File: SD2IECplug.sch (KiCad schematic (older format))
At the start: 46 parts, among them J1 ISP, J2 LED/SW, J3 SD_Card, J4 IEC, J5 C64-CassettePort, J6 C64-CassettePort, J7 USB_B, Q1 IRLML2803, Q2 IRLML2803, Q3 IRLML2803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

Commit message: Added optional I2C connector.
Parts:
- added J8: I2C, Pin_Headers:Pin_Header_Straight_1x04_Pitch2.54mm, symbol Conn_01x04
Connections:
- net labels added: SCL, SDA
- wire segments 111 -> 118
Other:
- moved on the sheet: D1, D2, J2, R1, R5

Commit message: Removed push button, added switch header.
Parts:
- removed SW1: DiskSwitch, Buttons_Switches_THT:SW_PUSH_6mm, symbol SW_Push
- added J9: SW, Pin_Headers:Pin_Header_Straight_1x06_Pitch2.54mm, symbol Conn_01x06
- J2: value LED/SW -> LED; symbol Conn_01x04 -> Conn_01x03
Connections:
- wire segments 118 -> 157
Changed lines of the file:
@@
 L GND #PWR017
 U 1 1 5A0E601A
-P 5250 4850
-F 0 "#PWR017" H 5250 4600 50  0001 C CNN
-F 1 "GND" H 5250 4700 50  0000 C CNN
-F 2 "" H 5250 4850 50  0001 C CNN
-F 3 "" H 5250 4850 50  0001 C CNN
-	1    5250 4850
-	1    0    0    -1
-$EndComp
-$Comp
-L SW_Push SW1
-U 1 1 5A0E643C
-P 4200 4800
-F 0 "SW1" H 4250 4900 50  0000 L CNN
-F 1 "DiskSwitch" H 4200 4740 50  0000 C CNN
-F 2 "Buttons_Switches_THT:SW_PUSH_6mm" H 4200 5000 50  0001 C CNN
-F 3 "" H 4200 5000 50  0001 C CNN
-	1    4200 4800
-	1    0    0    -1
-$EndComp
-$Comp
-L Conn_01x04 J2
+P 5400 4700
+F 0 "#PWR017" H 5400 4450 50  0001 C CNN
+F 1 "GND" H 5400 4550 50  0000 C CNN
+F 2 "" H 5400 4700 50  0001 C CNN
+F 3 "" H 5400 4700 50  0001 C CNN
+	1    5400 4700
+	1    0    0    -1
+$EndComp
+$Comp
+L Conn_01x03 J2
 U 1 1 5A0E6EA6
 P 5700 4250
 F 0 "J2" H 5700 4450 50  0000 C CNN
-F 1 "LED/SW" H 5700 3950 50  0000 C CNN
+F 1 "LED" H 5700 4050 50  0000 C CNN
 F 2 "Pin_Headers:Pin_Header_Straight_1x04_Pitch2.54mm" H 5700 4250 50  0001 C CNN
 F 3 "" H 5700 4250 50  0001 C CNN
@@
 SDA
 Wire Wire Line
-	9800 3650 9900 3650
+	9800 3650 9850 3650
+Wire Wire Line
+	9850 3650 9900 3650
 Connection ~ 9850 3650
 Wire Wire Line
-	9200 3950 10800 3950
+	9200 3950 9850 3950
+Wire Wire Line
+	9850 3950 10200 3950
+Wire Wire Line
+	10200 3950 10550 3950
+Wire Wire Line
+	10550 3950 10800 3950
 Connection ~ 10200 3950
 Wire Wire Line
@@
 	10800 3650 10800 3500
 Wire Wire Line
-	10500 3650 10800 3650
+	10500 3650 10550 3650
+Wire Wire Line
+	10550 3650 10800 3650
 Wire Wire Line
 	2100 6400 2100 6450
 Wire Wire Line
-	2100 6450 2400 6450
-Wire Wire Line
-	2400 6400 2400 6500
+	2100 6450 2200 6450
+Wire Wire Line
+	2200 6450 2300 6450
+Wire Wire Line
+	2300 6450 2400 6450
+Wire Wire Line
+	2400 6400 2400 6450
+Wire Wire Line
+	2400 6450 2400 6500
 Wire Wire Line
 	2300 6400 2300 6450
@@
 	2100 2400 2100 2350
 Wire Wire Line
-	2100 2350 2500 2350
+	2100 2350 2200 2350
+Wire Wire Line
+	2200 2350 2300 2350
+Wire Wire Line
+	2300 2350 2500 2350
 Wire Wire Line
 	2500 2350 2500 2400
@@
 Connection ~ 2200 2350
 Wire Wire Line
-	850  3100 850  3600
+	850  3100 850  3500
+Wire Wire Line
+	850  3500 850  3600
 Connection ~ 850  3500
 Wire Wire Line
-	1150 3100 1400 3100
-Wire Wire Line
-	1150 3500 1400 3500
+	1150 3100 1300 3100
+Wire Wire Line
+	1300 3100 1400 3100
+Wire Wire Line
+	1150 3500 1300 3500
+Wire Wire Line
+	1300 3500 1400 3500
 Wire Wire Line
 	1300 3450 1300 3500
@@
 Connection ~ 1300 3100
 Wire Wire Line
-	6800 1350 6800 1600
+	6800 1350 6800 1450
+Wire Wire Line
+	6800 1450 6800 1600
 Wire Wire Line
 	6800 1450 7050 1450
 Wire Wire Line
-	7050 1750 7050 2000
+	7050 1750 7050 1900
+Wire Wire Line
+	7050 1900 7050 2000
 Wire Wire Line
 	7050 2300 6800 2300
@@
 Connection ~ 6800 1450
 Wire Wire Line
-	5900 1350 5900 1600
+	5900 1350 5900 1450
+Wire Wire Line
+	5900 1450 5900 1600
 Wire Wire Line
 	5900 1450 6150 1450
 Wire Wire Line
-	6150 1750 6150 2000
+	6150 1750 6150 1900
+Wire Wire Line
+	6150 1900 6150 2000
 Wire Wire Line
 	6150 2300 5900 2300
@@
 Connection ~ 5900 1450
 Wire Wire Line
-	5000 1350 5000 1600
+	5000 1350 5000 1450
+Wire Wire Line
+	5000 1450 5000 1600
 Wire Wire Line
 	5000 1450 5250 1450
 Wire Wire Line
-	5250 1750 5250 2000
+	5250 1750 5250 1900
+Wire Wire Line
+	5250 1900 5250 2000
 Wire Wire Line
 	5250 2300 5000 2300
@@
 Connection ~ 5000 1450
 Wire Wire Line
-	4100 1350 4100 1600
+	4100 1350 4100 1450
+Wire Wire Line
+	4100 1450 4100 1600
 Wire Wire Line
 	4100 1450 4350 1450
 Wire Wire Line
-	4350 1750 4350 2000
+	4350 1750 4350 1900
+Wire Wire Line
+	4350 1900 4350 2000
 Wire Wire Line
 	4350 2300 4100 2300
@@
 	1400 2700 1400 1400
 Wire Wire Line
-	6150 3900 6150 4800
+	6150 3900 6150 4200
+Wire Wire Line
+	6150 4200 6150 4500
+Wire Wire Line
+	6150 4500 6150 4700
+Wire Wire Line
+	6150 4700 6150 4800
 Connection ~ 6150 4700
 Wire Wire Line
-	5950 4700 6400 4700
+	5950 4700 6150 4700
+Wire Wire Line
+	6150 4700 6400 4700
 Wire Wire Line
 	6400 3900 6150 3900
@@
 	3400 4000 6400 4000
 Wire Wire Line
-	4350 4500 5250 4500
-Wire Wire Line
-	5250 4350 5250 4850
-Connection ~ 5250 4600
-Wire Wire Line
-	4650 4600 4800 4600
-Wire Wire Line
-	3950 4500 4050 4500
-Wire Wire Line
-	5250 4800 4400 4800
-Connection ~ 5250 4800
-Wire Wire Line
-	3400 4800 4000 4800
-Wire Wire Line
-	3400 4500 3650 4500
-Wire Wire Line
-	3400 4600 4350 4600
+	4350 4500 5400 4500
+Wire Wire Line
+	5400 4350 5400 4500
+Wire Wire Line
+	5400 4500 5400 4600
+Wire Wire Line
+	5400 4600 5400 4700
+Connection ~ 5400 4600
+Wire Wire Line
+	4650 4600 4700 4600
+Wire Wire Line
+	4700 4600 4800 4600
+Wire Wire Line
+	3950 4500 4000 4500
+Wire Wire Line
+	4000 4500 4050 4500
+Wire Wire Line
+	3400 4500 3450 4500
+Wire Wire Line
+	3450 4500 3650 4500
+Wire Wire Line
+	3400 4600 3450 4600
+Wire Wire Line
+	3450 4600 4350 4600
 Connection ~ 4700 4600
 Connection ~ 4000 4500
 Wire Wire Line
-	5100 4600 5250 4600
-Wire Wire Line
-	5250 4350 5500 4350
-Connection ~ 5250 4500
+	5100 4600 5400 4600
+Wire Wire Line
+	5400 4350 5500 4350
+Connection ~ 5400 4500
 Wire Wire Line
 	4700 4600 4700 4250
@@
 	4000 4150 5500 4150
 Wire Wire Line
-	3950 4800 3950 5050
-Wire Wire Line
-	3950 5050 5500 5050
-Wire Wire Line
-	5500 5050 5500 4450
-Connection ~ 3950 4800
-Wire Wire Line
 	5950 4300 5950 3850
 Wire Wire Line
@@
 	8200 4400 8300 4400
 Wire Wire Line
-	8300 4400 8300 4800
+	8300 4400 8300 4500
+Wire Wire Line
+	8300 4500 8300 4800
 Wire Wire Line
 	3400 6000 8500 6000
@@
 	5750 7000 5850 7000
 Wire Wire Line
-	9300 5550 9400 5550
-Wire Wire Line
-	9300 6050 9400 6050
+	9300 5550 9350 5550
+Wire Wire Line
+	9350 5550 9400 5550
+Wire Wire Line
+	9300 6050 9350 6050
+Wire Wire Line
+	9350 6050 9400 6050
 Wire Wire Line
 	3400 5700 9350 5700
@@
 Connection ~ 9350 6050
 Wire Wire Line
-	9700 5550 9700 6200
+	9700 5550 9700 6050
+Wire Wire Line
+	9700 6050 9700 6200
 Connection ~ 9700 6050
 Wire Wire Line
-	11050 6150 11050 6300
+	11050 6150 11050 6250
+Wire Wire Line
+	11050 6250 11050 6300
 Wire Wire Line
 	10450 6150 10450 6250
@@
 Connection ~ 11050 5800
 Wire Wire Line
-	11050 5700 11050 5950
+	11050 5700 11050 5800
+Wire Wire Line
+	11050 5800 11050 5950
 Connection ~ 2400 6450
 Wire Wire Line
@@
 	3450 4550 3450 4600
 Connection ~ 3450 4600
+$Comp
+L Conn_01x06 J9
+U 1 1 5A18796D
+P 5100 5000
+F 0 "J9" H 5100 5300 50  0000 C CNN
+F 1 "SW" H 5100 4600 50  0000 C CNN
+F 2 "Pin_Headers:Pin_Header_Straight_1x06_Pitch2.54mm" H 5100 5000 50  0001 C CNN
+F 3 "" H 5100 5000 50  0001 C CNN
+	1    5100 5000
+	1    0    0    -1
+$EndComp
+Wire Wire Line
+	3400 4800 4900 4800
+Wire Wire Line
+	4900 4900 3400 4900
+Wire Wire Line
+	3400 5000 4900 5000
+Wire Wire Line
+	4900 5100 3400 5100
+Wire Wire Line
+	3400 5200 4900 5200
+$Comp
+L GND #PWR025
+U 1 1 5A187F94
+P 4800 5350
+F 0 "#PWR025" H 4800 5100 50  0001 C CNN
+F 1 "GND" H 4800 5200 50  0000 C CNN
+F 2 "" H 4800 5350 50  0001 C CNN
+F 3 "" H 4800 5350 50  0001 C CNN
+	1    4800 5350
+	1    0    0    -1
+$EndComp
+Wire Wire Line
+	4900 5300 4800 5300
+Wire Wire Line
+	4800 5300 4800 5350
 $EndSCHEMATC

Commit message: Forgotten changes.
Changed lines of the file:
@@
 SDA
 Wire Wire Line
-	9800 3650 9850 3650
-Wire Wire Line
-	9850 3650 9900 3650
+	9800 3650 9900 3650
 Connection ~ 9850 3650
 Wire Wire Line
-	9200 3950 9850 3950
-Wire Wire Line
-	9850 3950 10200 3950
-Wire Wire Line
-	10200 3950 10550 3950
-Wire Wire Line
-	10550 3950 10800 3950
+	9200 3950 10800 3950
 Connection ~ 10200 3950
 Wire Wire Line
@@
 	10800 3650 10800 3500
 Wire Wire Line
-	10500 3650 10550 3650
-Wire Wire Line
-	10550 3650 10800 3650
+	10500 3650 10800 3650
 Wire Wire Line
 	2100 6400 2100 6450
 Wire Wire Line
-	2100 6450 2200 6450
-Wire Wire Line
-	2200 6450 2300 6450
-Wire Wire Line
-	2300 6450 2400 6450
-Wire Wire Line
-	2400 6400 2400 6450
-Wire Wire Line
-	2400 6450 2400 6500
+	2100 6450 2400 6450
+Wire Wire Line
+	2400 6400 2400 6500
 Wire Wire Line
 	2300 6400 2300 6450
@@
 	2100 2400 2100 2350
 Wire Wire Line
-	2100 2350 2200 2350
-Wire Wire Line
-	2200 2350 2300 2350
-Wire Wire Line
-	2300 2350 2500 2350
+	2100 2350 2500 2350
 Wire Wire Line
 	2500 2350 2500 2400
@@
 Connection ~ 2200 2350
 Wire Wire Line
-	850  3100 850  3500
-Wire Wire Line
-	850  3500 850  3600
+	850  3100 850  3600
 Connection ~ 850  3500
 Wire Wire Line
-	1150 3100 1300 3100
-Wire Wire Line
-	1300 3100 1400 3100
-Wire Wire Line
-	1150 3500 1300 3500
-Wire Wire Line
-	1300 3500 1400 3500
+	1150 3100 1400 3100
+Wire Wire Line
+	1150 3500 1400 3500
 Wire Wire Line
 	1300 3450 1300 3500
@@
 Connection ~ 1300 3100
 Wire Wire Line
-	6800 1350 6800 1450
-Wire Wire Line
-	6800 1450 6800 1600
+	6800 1350 6800 1600
 Wire Wire Line
 	6800 1450 7050 1450
 Wire Wire Line
-	7050 1750 7050 1900
-Wire Wire Line
-	7050 1900 7050 2000
+	7050 1750 7050 2000
 Wire Wire Line
 	7050 2300 6800 2300
@@
 Connection ~ 6800 1450
 Wire Wire Line
-	5900 1350 5900 1450
-Wire Wire Line
-	5900 1450 5900 1600
+	5900 1350 5900 1600
 Wire Wire Line
 	5900 1450 6150 1450
 Wire Wire Line
-	6150 1750 6150 1900
-Wire Wire Line
-	6150 1900 6150 2000
+	6150 1750 6150 2000
 Wire Wire Line
 	6150 2300 5900 2300
@@
 Connection ~ 5900 1450
 Wire Wire Line
-	5000 1350 5000 1450
-Wire Wire Line
-	5000 1450 5000 1600
+	5000 1350 5000 1600
 Wire Wire Line
 	5000 1450 5250 1450
 Wire Wire Line
-	5250 1750 5250 1900
-Wire Wire Line
-	5250 1900 5250 2000
+	5250 1750 5250 2000
 Wire Wire Line
 	5250 2300 5000 2300
@@
 Connection ~ 5000 1450
 Wire Wire Line
-	4100 1350 4100 1450
-Wire Wire Line
-	4100 1450 4100 1600
+	4100 1350 4100 1600
 Wire Wire Line
 	4100 1450 4350 1450
 Wire Wire Line
-	4350 1750 4350 1900
-Wire Wire Line
-	4350 1900 4350 2000
+	4350 1750 4350 2000
 Wire Wire Line
 	4350 2300 4100 2300
@@
 	1400 2700 1400 1400
 Wire Wire Line
-	6150 3900 6150 4200
-Wire Wire Line
-	6150 4200 6150 4500
-Wire Wire Line
-	6150 4500 6150 4700
-Wire Wire Line
-	6150 4700 6150 4800
+	6150 3900 6150 4800
 Connection ~ 6150 4700
 Wire Wire Line
-	5950 4700 6150 4700
-Wire Wire Line
-	6150 4700 6400 4700
+	5950 4700 6400 4700
 Wire Wire Line
 	6400 3900 6150 3900
@@
 	4350 4500 5400 4500
 Wire Wire Line
-	5400 4350 5400 4500
-Wire Wire Line
-	5400 4500 5400 4600
-Wire Wire Line
-	5400 4600 5400 4700
+	5400 4350 5400 4700
 Connection ~ 5400 4600
 Wire Wire Line
-	4650 4600 4700 4600
-Wire Wire Line
-	4700 4600 4800 4600
-Wire Wire Line
-	3950 4500 4000 4500
-Wire Wire Line
-	4000 4500 4050 4500
-Wire Wire Line
-	3400 4500 3450 4500
-Wire Wire Line
-	3450 4500 3650 4500
-Wire Wire Line
-	3400 4600 3450 4600
-Wire Wire Line
-	3450 4600 4350 4600
+	4650 4600 4800 4600
+Wire Wire Line
+	3950 4500 4050 4500
+Wire Wire Line
+	3400 4500 3650 4500
+Wire Wire Line
+	3400 4600 4350 4600
 Connection ~ 4700 4600
 Connection ~ 4000 4500
@@
 	8200 4400 8300 4400
 Wire Wire Line
-	8300 4400 8300 4500
-Wire Wire Line
-	8300 4500 8300 4800
+	8300 4400 8300 4800
 Wire Wire Line
 	3400 6000 8500 6000
@@
 	5750 7000 5850 7000
 Wire Wire Line
-	9300 5550 9350 5550
-Wire Wire Line
-	9350 5550 9400 5550
-Wire Wire Line
-	9300 6050 9350 6050
-Wire Wire Line
-	9350 6050 9400 6050
+	9300 5550 9400 5550
+Wire Wire Line
+	9300 6050 9400 6050
 Wire Wire Line
 	3400 5700 9350 5700
@@
 Connection ~ 9350 6050
 Wire Wire Line
-	9700 5550 9700 6050
-Wire Wire Line
-	9700 6050 9700 6200
+	9700 5550 9700 6200
 Connection ~ 9700 6050
 Wire Wire Line
-	11050 6150 11050 6250
-Wire Wire Line
-	11050 6250 11050 6300
+	11050 6150 11050 6300
 Wire Wire Line
 	10450 6150 10450 6250
@@
 Connection ~ 11050 5800
 Wire Wire Line
-	11050 5700 11050 5800
-Wire Wire Line
-	11050 5800 11050 5950
+	11050 5700 11050 5950
 Connection ~ 2400 6450
 Wire Wire Line

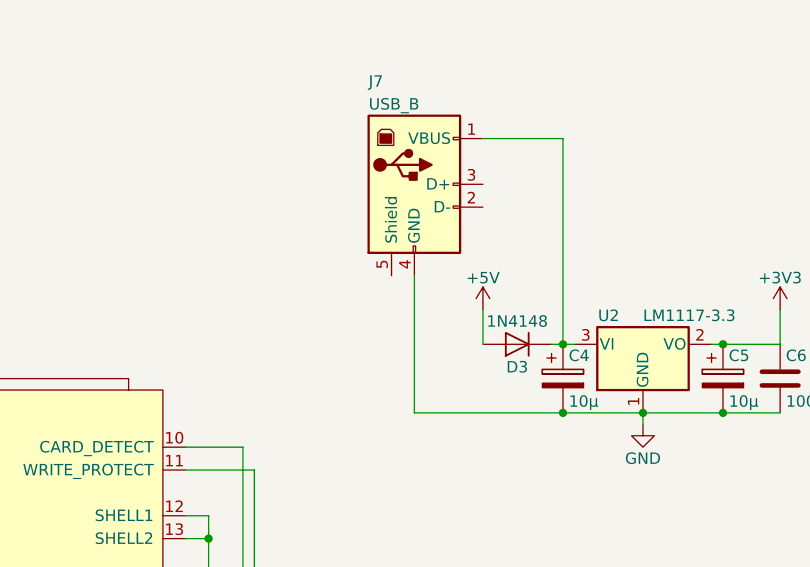
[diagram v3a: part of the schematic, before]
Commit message: Bug fix: Mini USB GND actually seems to be on pin 5.
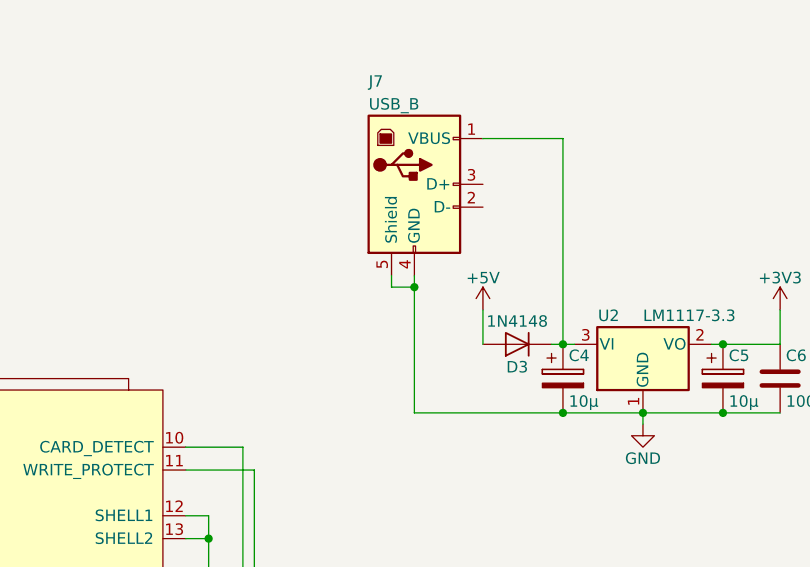
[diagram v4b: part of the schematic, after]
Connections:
- net GND: now also J7.5 (Shield)
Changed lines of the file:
@@
 Wire Wire Line
 	4800 5300 4800 5350
+Wire Wire Line
+	9100 3350 9100 3400
+Wire Wire Line
+	9100 3400 9200 3400
+Connection ~ 9200 3400
 $EndSCHEMATC

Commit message: Changed diode D3 footprint.
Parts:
- D3: footprint Diodes_SMD:D_SOD-323_HandSoldering -> Diodes_SMD:D_MicroMELF_Hadsoldering
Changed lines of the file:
@@
 F 0 "D3" H 9650 3750 50  0000 C CNN
 F 1 "1N4148" H 9650 3550 50  0000 C CNN
-F 2 "Diodes_SMD:D_SOD-323_HandSoldering" H 9650 3475 50  0001 C CNN
+F 2 "Diodes_SMD:D_MicroMELF_Hadsoldering" H 9650 3475 50  0001 C CNN
 F 3 "" H 9650 3650 50  0001 C CNN
 	1    9650 3650

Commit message: Upgraded project files.
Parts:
- C1, C2, C6: symbol C -> device:C
- C3, C4, C5: symbol CP -> device:CP
- D1, D2: symbol LED -> device:LED
- D3: symbol 1N4148 -> Diode:1N4148
- J1: symbol Conn_02x03_Odd_Even -> conn:Conn_02x03_Odd_Even
- J2: symbol Conn_01x03 -> conn:Conn_01x03
- J3: symbol SD_Card -> conn:SD_Card
- J4: symbol DIN-6 -> conn:DIN-6
- J5, J6: symbol C64-CassettePort -> hackup:C64-CassettePort
- J7: symbol USB_B -> conn:USB_B
- J8: symbol Conn_01x04 -> conn:Conn_01x04
- J9: symbol Conn_01x06 -> conn:Conn_01x06
- Q1, Q2, Q3, Q4: symbol IRLML2803 -> SD2IECplug:IRLML2803
- R1, R10, R11, R12, R13, R14, R15, R16, R17, R18, R19, R2, R20, R21, R3, R4, R5, R6, R7, R8, R9: symbol R -> device:R
- U1: symbol ATMEGA644-20AU -> atmel:ATMEGA644-20AU
- U2: symbol LM1117-3.3 -> regul:LM1117-3.3
- U3: symbol PC817 -> opto:PC817
- Y1: symbol Crystal -> device:Crystal

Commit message: First steps.
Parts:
- removed J2: LED, Pin_Headers:Pin_Header_Straight_1x04_Pitch2.54mm, symbol conn:Conn_01x03
- removed J7: USB_B, Connectors:USB_Mini-B, symbol conn:USB_B
- removed J8: I2C, Pin_Headers:Pin_Header_Straight_1x04_Pitch2.54mm, symbol conn:Conn_01x04
- removed J9: SW, Pin_Headers:Pin_Header_Straight_1x06_Pitch2.54mm, symbol conn:Conn_01x06
- removed R16, R17, R21: 10k, Capacitors_SMD:C_0805_HandSoldering, symbol device:R
- removed R18, R19: 22k, Capacitors_SMD:C_0805_HandSoldering, symbol device:R
- removed R20: 470, Capacitors_SMD:C_0805_HandSoldering, symbol device:R
- removed U3: PC817, hackup:SOP-4, symbol opto:PC817
- added J2: X6, Pin_Headers:Pin_Header_Straight_1x05_Pitch2.54mm, symbol conn:Conn_01x05
- added J7: Power, Pin_Headers:Pin_Header_Straight_1x02_Pitch2.54mm, symbol conn:Conn_01x02
- added J8: X3, Pin_Headers:Pin_Header_Straight_1x10_Pitch2.54mm, symbol conn:Conn_01x10
- D3: value 1N4148 -> 1N5817; footprint Diodes_SMD:D_MicroMELF_Hadsoldering -> Diodes_THT:D_DO-41_SOD81_P7.62mm_Horizontal
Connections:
- net labels added: DISKSWITCH, IEC_10-11, IEC_8-9, LED1, LED2, RESERVE
- net labels removed: SCL, SDA
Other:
- moved on the sheet: C3, C4, C5, C6, D3, J3, R15, U2

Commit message: First routing.
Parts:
- removed J3: SD_Card, SD-Connectors:SD-Connector-Short, symbol conn:SD_Card
- added XS1: SD Connector, lib:Conn_uSDcard, symbol uSD_push-push_ebay:SD_ebay-uSD-push_push_SMD
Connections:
- net labels added: WRITE_PROTECT
- wire segments 160 -> 154
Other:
- moved on the sheet: C3, R15
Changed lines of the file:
@@
 Text GLabel 1900 1300 2    39   BiDi ~ 0
 MOSI
-$Comp
-L conn:SD_Card J3
-U 1 1 5A0E2A2D
-P 9300 4300
-F 0 "J3" H 8650 4850 50  0000 C CNN
-F 1 "SD_Card" H 9900 3750 50  0000 C CNN
-F 2 "SD-Connectors:SD-Connector-Short" H 9500 4650 50  0001 C CNN
-F 3 "" H 9300 4300 50  0001 C CNN
-	1    9300 4300
-	1    0    0    -1
-$EndComp
-Text GLabel 8400 4600 0    39   Output ~ 0
+Text GLabel 8875 4450 0    39   Output ~ 0
 MISO
-Text GLabel 8400 4100 0    39   Input ~ 0
+Text GLabel 8875 3850 0    39   Input ~ 0
 MOSI
-Text GLabel 8400 4400 0    39   Input ~ 0
+Text GLabel 8875 3700 0    39   Input ~ 0
 SCK
-$Comp
-L power:GND #PWR014
-U 1 1 5A0E3997
-P 8150 4800
-F 0 "#PWR014" H 8150 4550 50  0001 C CNN
-F 1 "GND" H 8150 4650 50  0000 C CNN
-F 2 "" H 8150 4800 50  0001 C CNN
-F 3 "" H 8150 4800 50  0001 C CNN
-	1    8150 4800
-	1    0    0    -1
-$EndComp
 $Comp
 L power:GND #PWR015
 U 1 1 5A0E3F99
-P 10300 4800
-F 0 "#PWR015" H 10300 4550 50  0001 C CNN
-F 1 "GND" H 10300 4650 50  0000 C CNN
-F 2 "" H 10300 4800 50  0001 C CNN
-F 3 "" H 10300 4800 50  0001 C CNN
-	1    10300 4800
+P 9400 4850
+F 0 "#PWR015" H 9400 4600 50  0001 C CNN
+F 1 "GND" H 9400 4700 50  0000 C CNN
+F 2 "" H 9400 4850 50  0001 C CNN
+F 3 "" H 9400 4850 50  0001 C CNN
+	1    9400 4850
 	1    0    0    -1
 $EndComp
@@
 L power:+3V3 #PWR016
 U 1 1 5A0E48F3
-P 7950 3550
-F 0 "#PWR016" H 7950 3400 50  0001 C CNN
-F 1 "+3V3" H 7950 3690 50  0000 C CNN
-F 2 "" H 7950 3550 50  0001 C CNN
-F 3 "" H 7950 3550 50  0001 C CNN
-	1    7950 3550
+P 9400 3100
+F 0 "#PWR016" H 9400 2950 50  0001 C CNN
+F 1 "+3V3" H 9400 3240 50  0000 C CNN
+F 2 "" H 9400 3100 50  0001 C CNN
+F 3 "" H 9400 3100 50  0001 C CNN
+	1    9400 3100
 	1    0    0    -1
 $EndComp
@@
 L device:CP C3
 U 1 1 5A0E4A68
-P 7950 4450
-F 0 "C3" H 7975 4550 50  0000 L CNN
-F 1 "10µ" H 7975 4350 50  0000 L CNN
-F 2 "Capacitors_Tantalum_SMD:CP_Tantalum_Case-S_EIA-3216-12_Hand" H 7988 4300 50  0001 C CNN
-F 3 "" H 7950 4450 50  0001 C CNN
-	1    7950 4450
+P 8450 3750
+F 0 "C3" H 8475 3850 50  0000 L CNN
+F 1 "10µ" H 8475 3650 50  0000 L CNN
+F 2 "Capacitors_Tantalum_SMD:CP_Tantalum_Case-S_EIA-3216-12_Hand" H 8488 3600 50  0001 C CNN
+F 3 "" H 8450 3750 50  0001 C CNN
+	1    8450 3750
 	1    0    0    -1
 $EndComp
@@
 L device:R R15
 U 1 1 5A0E7D80
-P 7950 3700
-F 0 "R15" V 8030 3700 50  0000 C CNN
-F 1 "2.2R" V 7950 3700 50  0000 C CNN
-F 2 "Resistors_SMD:R_0805_HandSoldering" V 7880 3700 50  0001 C CNN
-F 3 "" H 7950 3700 50  0001 C CNN
-	1    7950 3700
+P 9400 3250
+F 0 "R15" V 9480 3250 50  0000 C CNN
+F 1 "2.2R" V 9400 3250 50  0000 C CNN
+F 2 "Resistors_SMD:R_0805_HandSoldering" V 9330 3250 50  0001 C CNN
+F 3 "" H 9400 3250 50  0001 C CNN
+	1    9400 3250
 	-1   0    0    1
 $EndComp
@@
 	1400 2700 1400 1400
 Wire Wire Line
-	8150 3900 8150 4200
-Connection ~ 8150 4700
-Wire Wire Line
-	7950 4700 8150 4700
-Wire Wire Line
-	8400 3900 8150 3900
-Wire Wire Line
-	8400 4200 8150 4200
-Connection ~ 8150 4200
-Wire Wire Line
-	8400 4500 8150 4500
-Connection ~ 8150 4500
-Wire Wire Line
-	10200 4500 10300 4500
-Connection ~ 10300 4500
-Wire Wire Line
-	7950 4300 8400 4300
-Wire Wire Line
-	7950 4600 7950 4700
-Wire Wire Line
 	4350 4500 5400 4500
 Wire Wire Line
 	5100 4600 5400 4600
-Wire Wire Line
-	7950 4300 7950 3850
-Wire Wire Line
-	10200 4400 10300 4400
-Wire Wire Line
-	10300 4400 10300 4500
-Wire Wire Line
-	10500 6000 10500 4200
-Wire Wire Line
-	10500 4200 10200 4200
-Wire Wire Line
-	10450 5600 10450 4100
-Wire Wire Line
-	10450 4100 10200 4100
 Wire Wire Line
 	5750 6800 5850 6800
@@
 Wire Wire Line
 	4100 1450 4100 1600
-Wire Wire Line
-	8150 4700 8150 4800
-Wire Wire Line
-	8150 4700 8400 4700
-Wire Wire Line
-	8150 4200 8150 4500
-Wire Wire Line
-	8150 4500 8150 4700
-Wire Wire Line
-	10300 4500 10300 4800
 Wire Wire Line
 	2400 6450 2400 6500
@@
 Connection ~ 9500 2700
 Connection ~ 10450 2400
-Connection ~ 7950 4300
-Wire Wire Line
-	3400 4000 8400 4000
-Wire Wire Line
-	3400 5600 10450 5600
-Wire Wire Line
-	3400 6000 10500 6000
 $Comp
 L conn:Conn_01x10 J8
@@
 Wire Wire Line
 	3400 4600 4350 4600
+$Comp
+L uSD_push-push_ebay:SD_ebay-uSD-push_push_SMD XS1
+U 1 1 5B9B7C9E
+P 9250 4150
+F 0 "XS1" H 8945 4196 50  0000 R CNN
+F 1 "SD Connector" H 9850 4900 50  0000 R CNN
+F 2 "lib:Conn_uSDcard" H 9250 4150 10  0001 C CNN
+F 3 "_" H 9250 4150 10  0001 C CNN
+F 4 "_" H 9250 4150 10  0001 C CNN "Manf#"
+F 5 "ebay" H 9250 4150 10  0001 C CNN "Manf"
+	1    9250 4150
+	-1   0    0    -1
+$EndComp
+Wire Wire Line
+	9400 3400 9400 3475
+Wire Wire Line
+	9400 4775 9400 4800
+Wire Wire Line
+	3400 5600 8700 5600
+Wire Wire Line
+	3400 4000 8875 4000
+Wire Wire Line
+	8450 3900 8450 4300
+Wire Wire Line
+	8450 4300 8875 4300
+Wire Wire Line
+	8450 3600 8450 3475
+Wire Wire Line
+	8450 3475 9400 3475
+Connection ~ 9400 3475
+Wire Wire Line
+	9400 3475 9400 3525
+Wire Wire Line
+	8700 4600 8875 4600
+Wire Wire Line
+	8700 4600 8700 5600
+Wire Wire Line
+	8875 4150 8575 4150
+Wire Wire Line
+	8575 4150 8575 4800
+Wire Wire Line
+	8575 4800 9400 4800
+Connection ~ 9400 4800
+Wire Wire Line
+	9400 4800 9400 4850
+$Comp
+L power:GND #PWR0103
+U 1 1 5BA175F3
+P 3575 6175
+F 0 "#PWR0103" H 3575 5925 50  0001 C CNN
+F 1 "GND" H 3575 6025 50  0000 C CNN
+F 2 "" H 3575 6175 50  0001 C CNN
+F 3 "" H 3575 6175 50  0001 C CNN
+	1    3575 6175
+	1    0    0    -1
+$EndComp
+Wire Wire Line
+	3400 6000 3575 6000
+Wire Wire Line
+	3575 6000 3575 6175
+Text Label 3400 6000 0    39   ~ 0
+WRITE_PROTECT
 $EndSCHEMATC
